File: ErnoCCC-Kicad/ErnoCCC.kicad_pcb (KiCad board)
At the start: 2 copper layers, 161.4 x 95.9 mm, 96 parts, among them J1 6VAC, J2 ICSP, J3 FTDI, J4 Erno Controller, J5 SWITCH, J6 LED OUT, J7 Conn_01x05, Q1 BC847, Q2 BC847, SW1 SW_Push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

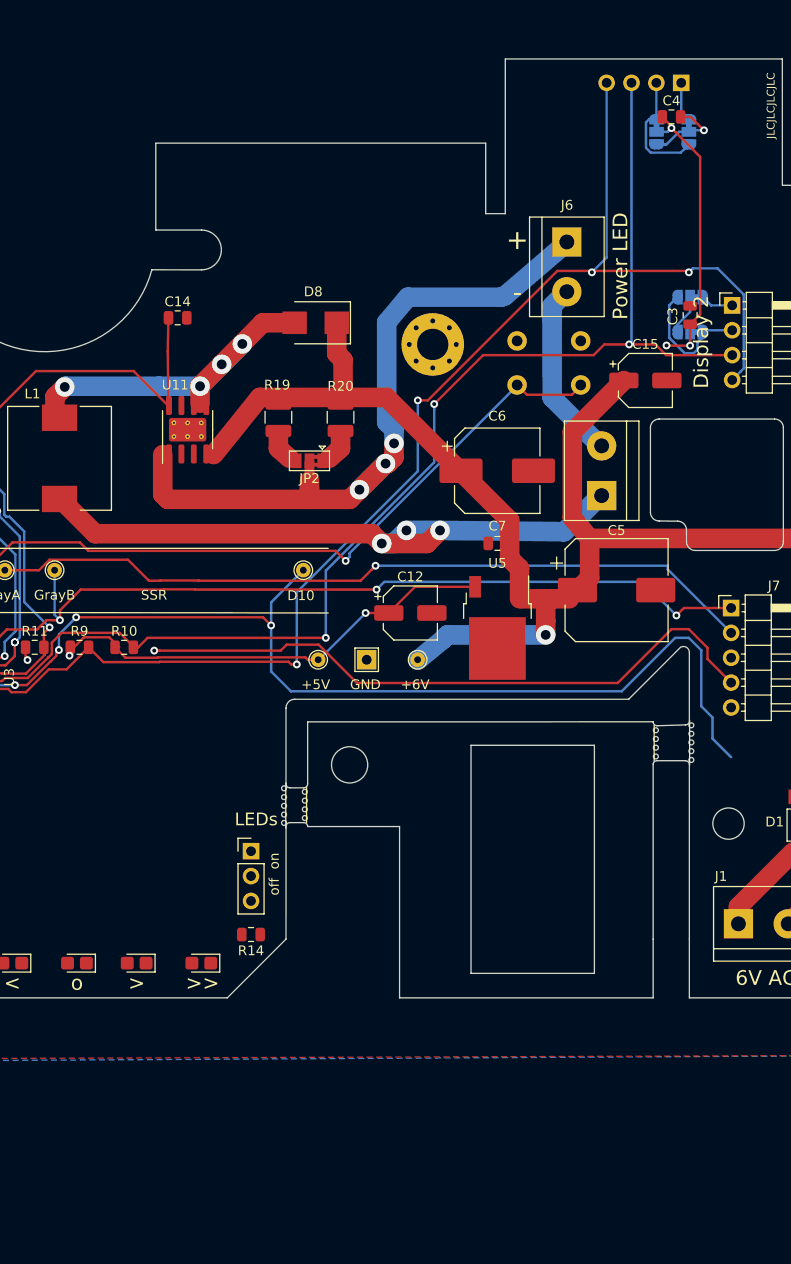
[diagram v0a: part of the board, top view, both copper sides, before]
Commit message: Updating the Pin Header Length (6x done, 4x and 7x to follow)
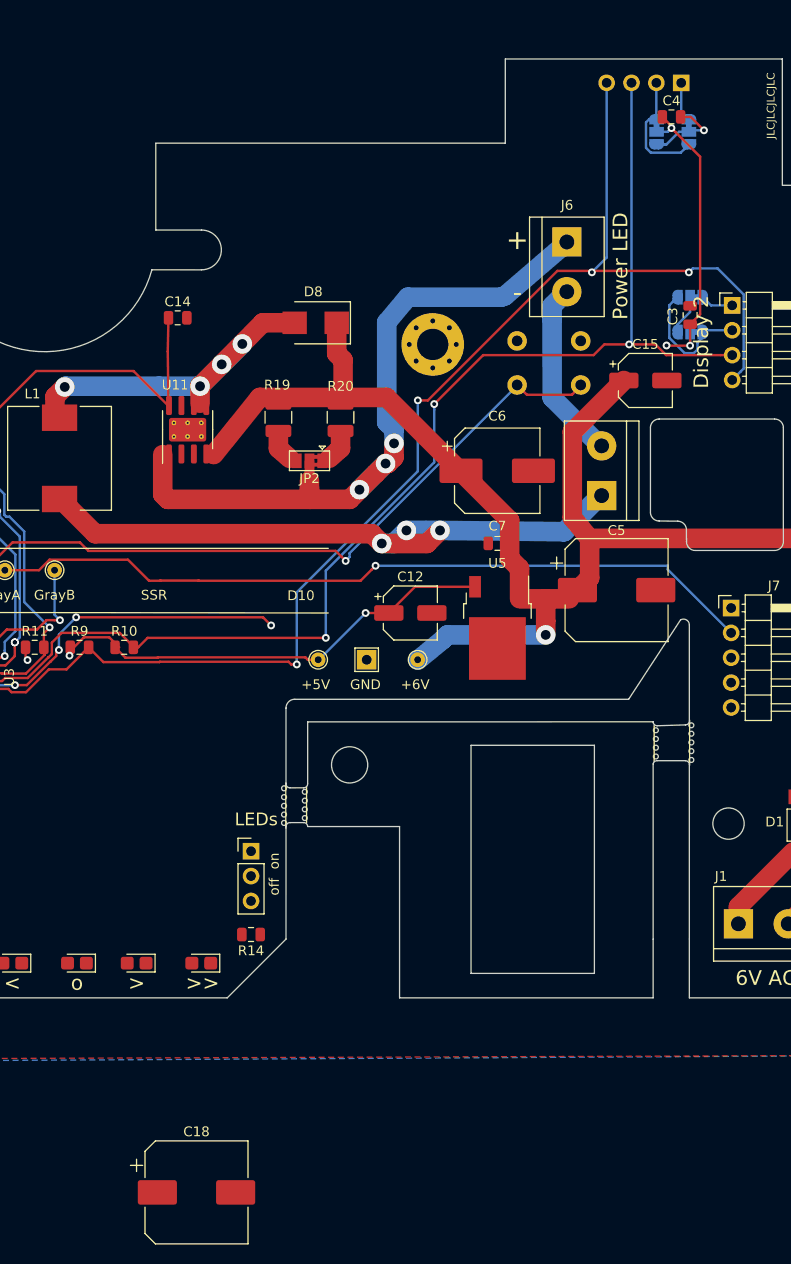
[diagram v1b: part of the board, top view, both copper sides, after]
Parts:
- removed TP15: D10, TestPoint:TestPoint_THTPad_D1.5mm_Drill0.7mm
- added C18: 470u, Capacitor_SMD:CP_Elec_10x10, F.Cu at (159.3, 141.0)
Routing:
- net /GRAY-A: track 140.4 -> 67.7 mm, vias 7 -> 5
- net /D10: track 113.1 -> 41.6 mm
- net /D9: track 66.2 -> 0.00 mm, vias 1 -> 0
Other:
- outline, holes or cut-outs redrawn

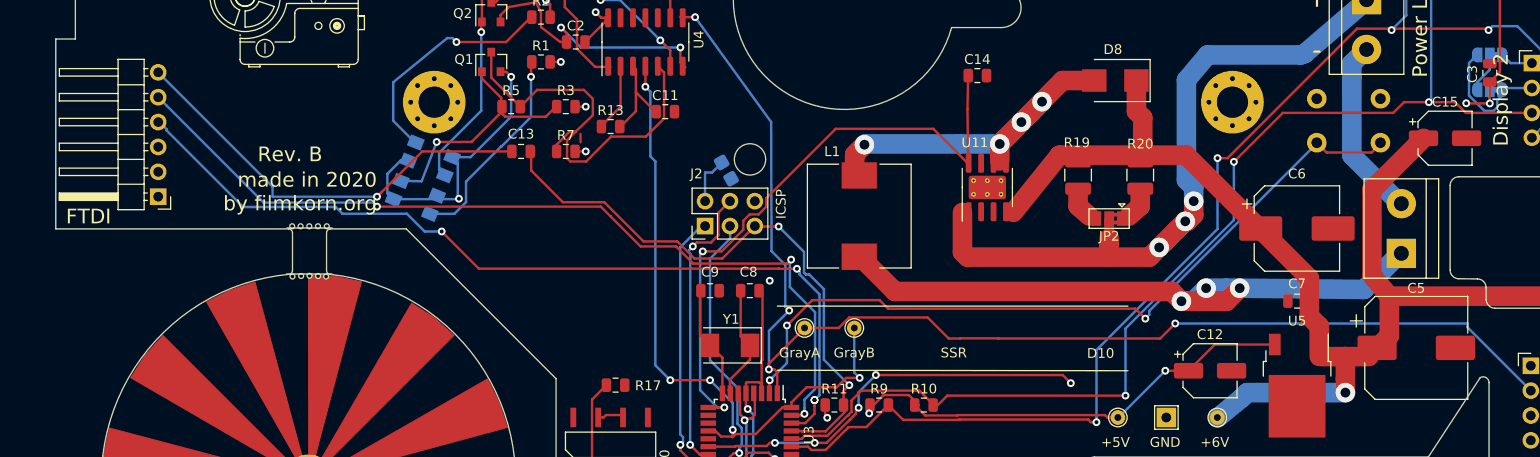
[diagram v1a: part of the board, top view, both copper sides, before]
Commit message: Updating QRE1113 footrpint
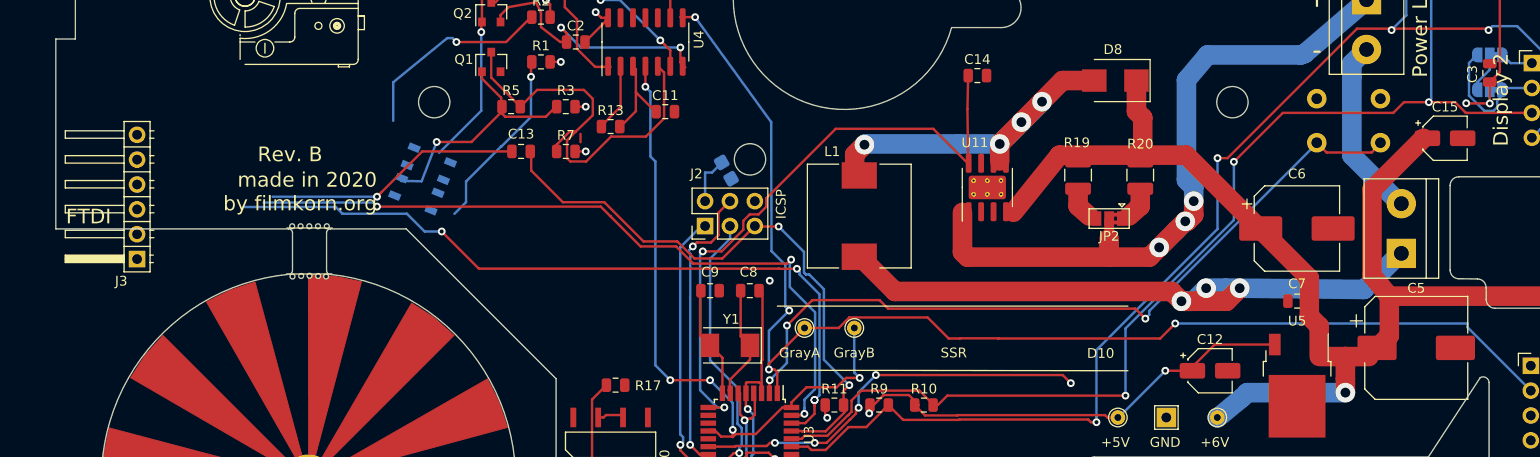
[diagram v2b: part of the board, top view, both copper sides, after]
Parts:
- C12, C15: footprint Capacitor_SMD:CP_Elec_5x5.8 -> Capacitor_SMD:CP_Elec_4x4.5
- J3: footprint Connector_PinHeader_2.54mm:PinHeader_1x06_P2.54mm_Horizontal -> Connector_PinHeader_2.54mm:PinHeader_1x06_P2.54mm_Horizontal_shorter
- REF** (x2): value MountingHole_3.2mm_M3_Pad_Via -> MountingHole_3.2mm_M3; footprint MountingHole:MountingHole_3.2mm_M3_Pad_Via -> MountingHole:MountingHole_3.2mm_M3
- U1, U2: footprint ErnoCCC:QRE1113GR -> ErnoCCC:QRE1113GR-slim
- moved U2 0.26 mm to (101.4, 60.4)
- moved U1 0.08 mm to (99.9, 64.0)
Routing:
- net GND: track 102.3 -> 72.1 mm, vias 9 -> 7
- net Net-(C13-Pad1): track 43.9 -> 26.4 mm
- net /TX: track 91.1 -> 75.4 mm
- net /RX: track 90.5 -> 78.2 mm
- net Net-(R2-Pad2): track 24.4 -> 20.8 mm
- net Net-(Q2-Pad1): track 38.6 -> 35.5 mm
- net Net-(R1-Pad2): track 21.3 -> 18.8 mm

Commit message: Smaller Header footprint for 4 & 5 pin connectors
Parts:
- D9: footprint Connector_PinHeader_2.54mm:PinHeader_1x04_P2.54mm_Horizontal -> Connector_PinHeader_2.54mm:PinHeader_1x04_P2.54mm_Horizontal_shorter
- J7: footprint Connector_PinHeader_2.54mm:PinHeader_1x05_P2.54mm_Horizontal -> Connector_PinHeader_2.54mm:PinHeader_1x05_P2.54mm_Horizontal_shorter

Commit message: Correcting Display Position
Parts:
- moved D7 1.44 mm to (207.6, 26.8)
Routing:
- net /SCL: track 126.6 -> 99.9 mm
- net /SDA: track 135.3 -> 117.5 mm
- net Net-(D7-Pad1): track 4.03 -> 0.00 mm
- net Net-(D7-Pad2): track 12.5 -> 8.74 mm
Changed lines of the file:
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@@
     (thickness 1.6)
     (drawings 300)
-    (tracks 689)
+    (tracks 682)
     (zones 0)
     (modules 96)
@@
   )
   (module Connector_PinHeader_2.54mm:PinHeader_1x04_P2.54mm_Vertical (layer B.Cu)
-    (at 208.77 27.636 90)
+    (at 207.6 26.8 90)
     (descr "Through hole straight pin header, 1x04, 2.54mm pitch, single row")
     (tags "Through hole pin header THT 1x04 2.54mm single row")
@@
   (via (at 199.644 46.99) (size 0.8) (drill 0.4) (layers F.Cu B.Cu) (net 22))
   (segment (start 201.15 45.484) (end 199.644 46.99) (width 0.25) (layer B.Cu) (net 22))
-  (segment (start 201.15 27.636) (end 201.15 45.484) (width 0.25) (layer B.Cu) (net 22))
   (segment (start 139.394 88.742) (end 139.707003 88.428997) (width 0.25) (layer F.Cu) (net 23))
   (segment (start 144.129164 86.31901) (end 144.14684 86.31901) (width 0.25) (layer F.Cu) (net 23))
@@
   (segment (start 183.537984 60.448338) (end 188.537322 55.449) (width 0.25) (layer F.Cu) (net 23))
   (segment (start 188.537322 55.449) (end 199.821 55.449) (width 0.25) (layer F.Cu) (net 23))
-  (segment (start 203.69 27.636) (end 203.69 53.993) (width 0.25) (layer B.Cu) (net 23))
   (segment (start 203.454 54.229) (end 203.454 54.356) (width 0.25) (layer B.Cu) (net 23))
   (segment (start 203.454 54.356) (end 206.135338 54.356) (width 0.25) (layer F.Cu) (net 23))
   (via (at 203.454 54.356) (size 0.8) (drill 0.4) (layers F.Cu B.Cu) (net 23))
-  (segment (start 203.69 53.993) (end 203.454 54.229) (width 0.25) (layer B.Cu) (net 23))
   (segment (start 200.914 54.356) (end 203.454 54.356) (width 0.25) (layer F.Cu) (net 23))
   (segment (start 143.6675 85.294) (end 143.6675 83.8485) (width 0.25) (layer F.Cu) (net 24))
@@
   (segment (start 144.745888 82.521897) (end 145.311573 82.521897) (width 0.25) (layer F.Cu) (net 55))
   (via (at 145.311573 82.521897) (size 0.8) (drill 0.4) (layers F.Cu B.Cu) (net 55))
-  (segment (start 208.77 30.559) (end 209.55 31.339) (width 0.25) (layer B.Cu) (net 56))
-  (segment (start 208.77 27.636) (end 208.77 30.559) (width 0.25) (layer B.Cu) (net 56))
-  (segment (start 206.23 31.321) (end 206.248 31.339) (width 0.25) (layer B.Cu) (net 57))
-  (segment (start 206.23 27.636) (end 206.23 31.321) (width 0.25) (layer B.Cu) (net 57))
   (segment (start 209.095936 34.393064) (end 209.55 33.939) (width 0.25) (layer B.Cu) (net 57))
   (segment (start 208.72499 34.76401) (end 209.095936 34.393064) (width 0.25) (layer B.Cu) (net 57))

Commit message: Fixing Schematics Bugs, PCB progress
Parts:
- moved C5 0.67 mm to (201.7, 79.0)
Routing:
- net /GRAY-B: track 129.7 -> 120.2 mm
- net +6V: track 151.0 -> 145.7 mm
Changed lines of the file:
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@@
     (thickness 1.6)
     (drawings 300)
-    (tracks 682)
+    (tracks 683)
     (zones 0)
     (modules 96)
@@
   )
   (module Capacitor_SMD:CP_Elec_10x10 (layer F.Cu)
-    (at 202.166 79.452)
+    (at 201.676 78.994)
     (descr "SMD capacitor, aluminum electrolytic, Nichicon, 10.0x10.0mm")
     (tags "capacitor electrolytic")
@@
   (segment (start 194.927 84.024) (end 184.894 84.024) (width 2) (layer B.Cu) (net 44))
   (segment (start 197.641999 72.038999) (end 199.39 74.168) (width 2) (layer F.Cu) (net 44))
-  (segment (start 221.742 74.168) (end 199.39 74.168) (width 2) (layer F.Cu) (net 44))
-  (segment (start 222.758 75.184) (end 221.742 74.168) (width 2) (layer F.Cu) (net 44))
-  (segment (start 222.758 100.566001) (end 222.758 75.184) (width 2) (layer F.Cu) (net 44))
   (segment (start 197.34 80.341) (end 194.927 80.341) (width 2) (layer F.Cu) (net 44))
-  (segment (start 199.416 78.202) (end 199.416 74.194) (width 2) (layer F.Cu) (net 44))
   (segment (start 199.416 74.194) (end 199.39 74.168) (width 2) (layer F.Cu) (net 44))
   (segment (start 198.166 79.452) (end 199.416 78.202) (width 2) (layer F.Cu) (net 44))
+  (segment (start 208.221809 75.946) (end 199.39 75.946) (width 2) (layer F.Cu) (net 44))
+  (segment (start 209.200819 76.92501) (end 208.221809 75.946) (width 2) (layer F.Cu) (net 44))
+  (segment (start 216.681612 76.92501) (end 209.200819 76.92501) (width 2) (layer F.Cu) (net 44))
+  (segment (start 222.758 83.001398) (end 216.681612 76.92501) (width 2) (layer F.Cu) (net 44))
+  (segment (start 222.758 100.566001) (end 222.758 83.001398) (width 2) (layer F.Cu) (net 44))
+  (segment (start 199.39 75.946) (end 199.416 74.194) (width 2) (layer F.Cu) (net 44))
+  (segment (start 199.416 78.202) (end 199.39 75.946) (width 2) (layer F.Cu) (net 44))
   (segment (start 167.622 63.704) (end 167.622 64.974) (width 2) (layer F.Cu) (net 45))
   (segment (start 167.622 64.974) (end 168.765 65.99) (width 2) (layer F.Cu) (net 45))
@@
   (segment (start 136.307998 69.568534) (end 137.714958 70.975494) (width 0.25) (layer B.Cu) (net 54))
   (segment (start 128.506 45.67) (end 136.271 56.388) (width 0.25) (layer B.Cu) (net 54))
-  (via (at 177.546 76.962) (size 0.8) (drill 0.4) (layers F.Cu B.Cu) (net 54))
-  (segment (start 177.546 76.962) (end 207.391 76.962) (width 0.25) (layer B.Cu) (net 54))
-  (segment (start 207.391 77.343) (end 213.868 83.82) (width 0.25) (layer B.Cu) (net 54))
-  (segment (start 207.391 76.962) (end 207.391 77.343) (width 0.25) (layer B.Cu) (net 54))
-  (segment (start 139.682 77.42) (end 143.170998 77.42) (width 0.25) (layer F.Cu) (net 54))
-  (segment (start 143.170998 77.42) (end 144.245999 76.344999) (width 0.25) (layer F.Cu) (net 54))
-  (segment (start 159.465976 78.474978) (end 159.485999 78.495001) (width 0.25) (layer F.Cu) (net 54))
-  (segment (start 144.245999 76.344999) (end 152.255997 76.344999) (width 0.25) (layer F.Cu) (net 54))
-  (segment (start 159.485999 78.495001) (end 176.012999 78.495001) (width 0.25) (layer F.Cu) (net 54))
-  (segment (start 152.255997 76.344999) (end 154.405999 78.495001) (width 0.25) (layer F.Cu) (net 54))
-  (segment (start 177.146001 77.361999) (end 177.546 76.962) (width 0.25) (layer F.Cu) (net 54))
-  (segment (start 154.405999 78.495001) (end 155.563177 78.495001) (width 0.25) (layer F.Cu) (net 54))
-  (segment (start 155.563177 78.495001) (end 155.5832 78.474978) (width 0.25) (layer F.Cu) (net 54))
-  (segment (start 155.5832 78.474978) (end 159.465976 78.474978) (width 0.25) (layer F.Cu) (net 54))
   (segment (start 176.012999 78.495001) (end 177.146001 77.361999) (width 0.25) (layer F.Cu) (net 54))
+  (segment (start 155.5832 78.474978) (end 159.465976 78.474978) (width 0.25) (layer F.Cu) (net 54))
+  (segment (start 155.563177 78.495001) (end 155.5832 78.474978) (width 0.25) (layer F.Cu) (net 54))
+  (segment (start 154.405999 78.495001) (end 155.563177 78.495001) (width 0.25) (layer F.Cu) (net 54))
+  (segment (start 177.146001 77.361999) (end 177.546 76.962) (width 0.25) (layer F.Cu) (net 54))
+  (segment (start 152.255997 76.344999) (end 154.405999 78.495001) (width 0.25) (layer F.Cu) (net 54))
+  (segment (start 159.485999 78.495001) (end 176.012999 78.495001) (width 0.25) (layer F.Cu) (net 54))
+  (segment (start 144.245999 76.344999) (end 152.255997 76.344999) (width 0.25) (layer F.Cu) (net 54))
+  (segment (start 159.465976 78.474978) (end 159.485999 78.495001) (width 0.25) (layer F.Cu) (net 54))
+  (segment (start 143.170998 77.42) (end 144.245999 76.344999) (width 0.25) (layer F.Cu) (net 54))
+  (segment (start 139.682 77.42) (end 143.170998 77.42) (width 0.25) (layer F.Cu) (net 54))
+  (segment (start 177.546 76.962) (end 207.391 76.962) (width 0.25) (layer B.Cu) (net 54))
+  (via (at 177.546 76.962) (size 0.8) (drill 0.4) (layers F.Cu B.Cu) (net 54))
   (segment (start 129.844 87.942) (end 129.922 87.942) (width 0.25) (layer F.Cu) (net 55))
   (via (at 125.966 82.754) (size 0.8) (drill 0.4) (layers F.Cu B.Cu) (net 55))

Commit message: Spreading out parts
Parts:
- removed TP4: GRAY-B, TestPoint:TestPoint_THTPad_D1.5mm_Drill0.7mm
- removed TP5: GRAY-A, TestPoint:TestPoint_THTPad_D1.5mm_Drill0.7mm
- moved R15 78.3 mm to (141.7, 96.3)
- moved RV1 75.1 mm to (149.4, 100.8), turned to 270 degrees
- moved R18 70.5 mm to (143.8, 105.2)
- moved R16 64.9 mm to (143.8, 100.3), turned to 180 degrees
- moved U6 63.9 mm to (139.4, 100.3), turned to 90 degrees
- moved C17 59.0 mm to (133.6, 105.2)
- moved C18 55.9 mm to (121.7, 99.6)
- moved U7 55.6 mm to (133.6, 100.3), turned to 90 degrees
- moved C16 53.5 mm to (138.7, 105.2)
- moved R17 16.8 mm to (131.1, 96.3)
- moved U9 13.9 mm to (120.4, 87.6)
- moved U10 11.6 mm to (120.4, 77.7)
- moved JP1 10.5 mm to (162.3, 96.0)
- moved R14 10.5 mm to (162.3, 104.5)
- moved D2 9.71 mm to (141.0, 110.4)
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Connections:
- U7 pad 1: /VCTRL -> /DAC
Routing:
- net /GRAY-B: track 120.2 -> 0.00 mm, vias 4 -> 0
- net /BTTN: track 78.9 -> 40.4 mm
- net Net-(R17-Pad1): track 20.8 -> 0.00 mm
- net GND: track 72.1 -> 61.2 mm, vias 7 -> 6
- net /GRAY-A: track 67.7 -> 62.4 mm
- net Net-(J4-Pad4): track 2.39 -> 0.00 mm
- net Net-(J4-Pad2): track 2.39 -> 0.00 mm
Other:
- outline, holes or cut-outs redrawn
- board text added: "+15 VDC"
- board text added: "Blue"
- board text added: "Orange"
- board text removed: "Bl. PCB"
- board text removed: "Bl. Pot"
- board text removed: "D10"
- board text removed: "GrayA"
- board text removed: "GrayB"
- board text removed: "Or. PCB"
- board text removed: "Or. Pot"
- board text removed: "SSR"

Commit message: Re-Routed 99%
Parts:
- moved R16 12.8 mm to (131.8, 104.9)
- moved RV1 3.61 mm to (147.1, 98.0)
- moved C16 3.57 mm to (142.2, 104.9)
- moved C17 3.57 mm to (137.2, 104.9)
- moved R18 3.57 mm to (147.3, 104.9)
- turned U6 to 270 degrees
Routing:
- net /GRAY-B: track 0.00 -> 127.7 mm, vias 0 -> 3
- net /SSR: track 0.00 -> 103.9 mm, vias 0 -> 2
- net /D9: track 0.00 -> 96.3 mm, vias 0 -> 3
- net Net-(D10-Pad1): track 0.00 -> 85.2 mm, vias 0 -> 1
- net /GRAY-A: track 62.4 -> 136.2 mm, vias 5 -> 7
- net /D10: track 41.6 -> 100.1 mm, vias 5 -> 4
- net />>: track 0.00 -> 54.0 mm, vias 0 -> 2
- net Net-(J4-Pad5): track 0.00 -> 40.0 mm, vias 0 -> 1
- net /VCTRL: track 0.00 -> 39.9 mm, vias 0 -> 2
- net Net-(J4-Pad6): track 0.00 -> 39.8 mm, vias 0 -> 1
- net +15V: track 0.00 -> 39.5 mm
- net /BTTN: track 40.4 -> 75.8 mm
- net />: track 0.00 -> 33.1 mm, vias 0 -> 2
- net Net-(J4-Pad4): track 0.00 -> 28.0 mm, vias 0 -> 1
- net /o: track 0.00 -> 27.4 mm, vias 0 -> 2
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
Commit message: Wiring it all up
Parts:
- moved D9 1.96 mm to (214.1, 52.3)
- moved REF** 0.57 mm to (183.6, 53.8)
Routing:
- net /SCL: track 99.9 -> 129.0 mm
- net /SDA: track 117.5 -> 145.4 mm
- net Net-(C13-Pad1): track 26.4 -> 46.1 mm
- net /TX: track 75.4 -> 93.6 mm
- net GND: track 79.2 -> 97.1 mm, vias 6 -> 7
- net /RX: track 78.2 -> 93.5 mm
- net /GRAY-B: track 127.7 -> 135.3 mm
- net /D9: track 96.3 -> 102.5 mm, vias 3 -> 1
- net /GRAY-A: track 136.2 -> 141.6 mm, vias 7 -> 6
- net Net-(D7-Pad1): track 0.00 -> 5.40 mm
- net Net-(R2-Pad2): track 20.8 -> 26.1 mm
- net Net-(D7-Pad2): track 8.74 -> 13.7 mm
- net /D10: track 100.1 -> 104.5 mm, vias 4 -> 1
- net Net-(D9-Pad2): track 13.3 -> 17.1 mm
- net Net-(D9-Pad1): track 3.35 -> 7.10 mm
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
